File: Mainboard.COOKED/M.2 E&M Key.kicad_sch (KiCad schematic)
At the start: 26 parts, among them J15 Bus_M.2_Socket_M, J16 Bus_M.2_Socket_E

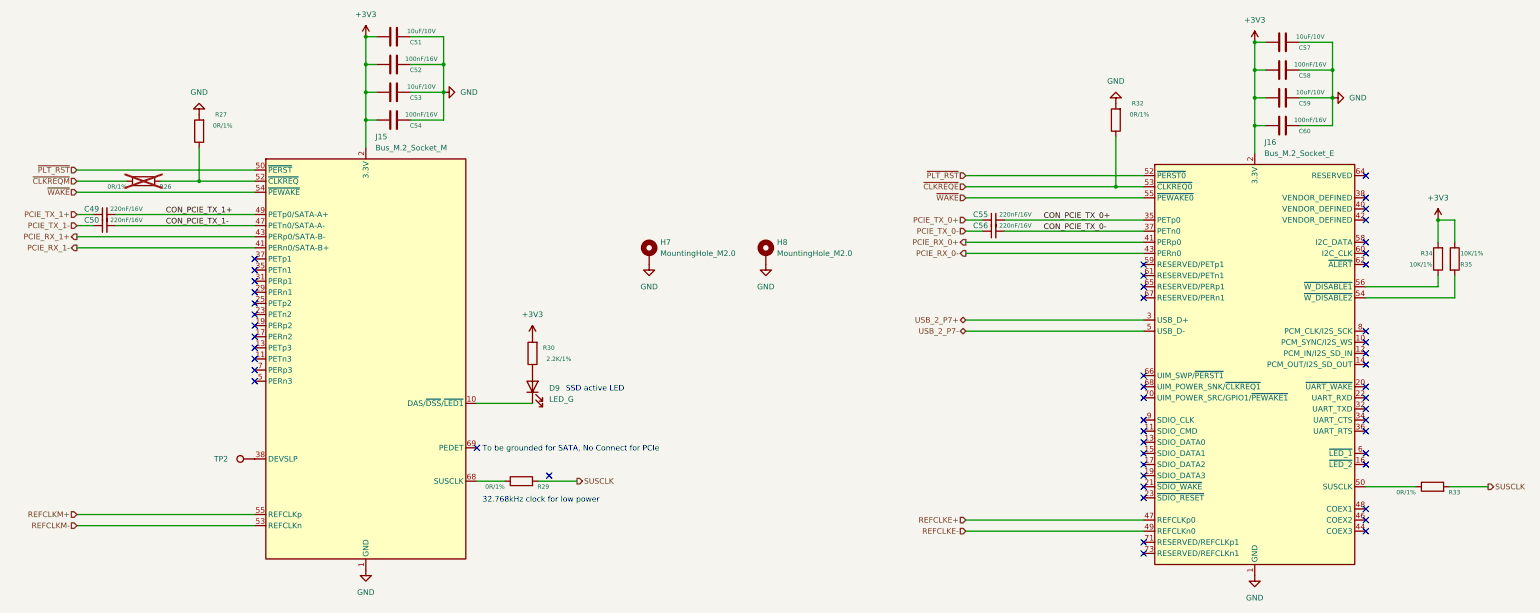
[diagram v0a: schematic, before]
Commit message: "Scrapped" the current Mainboard, seems to be very broken for no reason.
It is being kept for now so that work done for the displays can be copied over later.
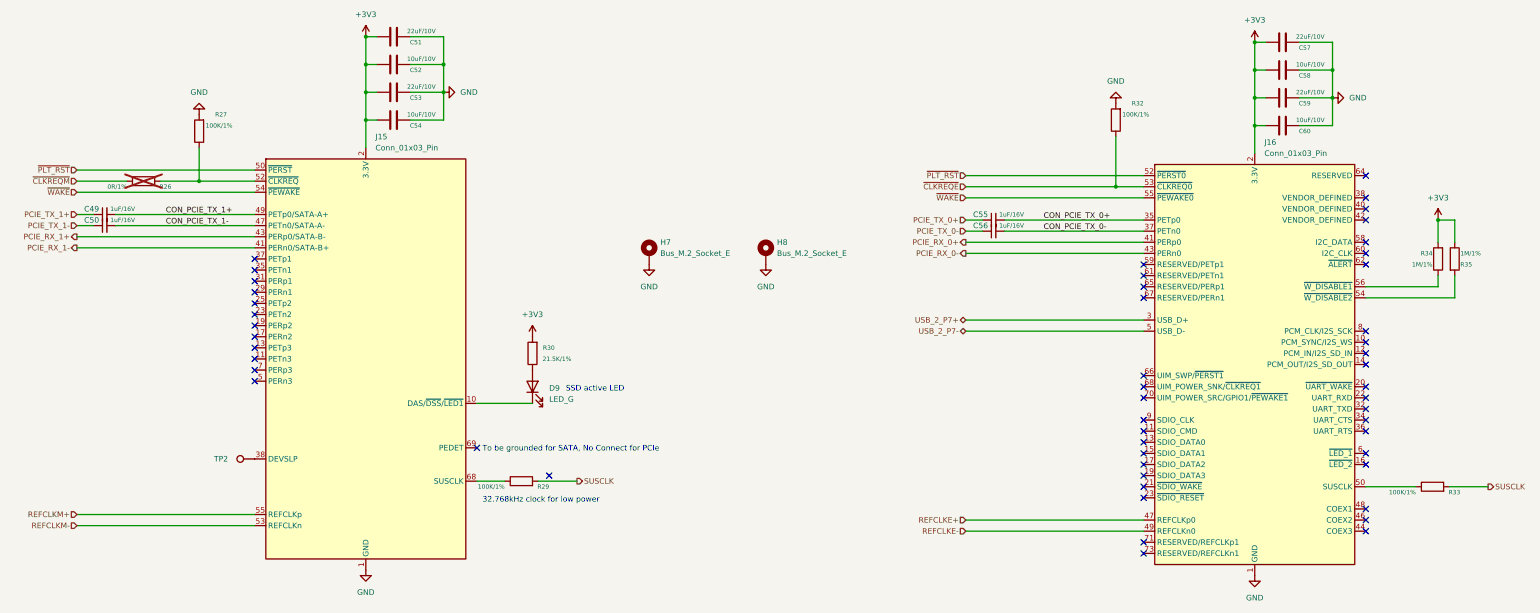
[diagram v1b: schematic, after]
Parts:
- C49, C50, C55, C56: value 220nF/16V -> 1uF/16V; Buy_Link https://item.szlcsc.com/137804.html -> (none); DF_Comment 贴片电容0402-220nF-16V-X7R -> 贴片电容0402-1uF-16V-X5R(0402)
- C51, C53, C57, C59: value 10uF/10V -> 22uF/10V; footprint A_HDJ_Library:C_0402_1005Metric -> A_HDJ_Library:C_0603_1608Metric; DF_Comment 贴片电容0402-10UF-10V-X5R_GRM155R61A106ME44D -> 贴片电容0603-22uF-10V-X5R(0603); SCH_Show_Footprint C0402 -> C603
- C52, C54, C58, C60: value 100nF/16V -> 10uF/10V; DF_Comment 贴片电容0402-100nF-16V-X7R(0402) -> 贴片电容0402-10UF-10V-X5R_GRM155R61A106ME44D; SCH_Show_Footprint C0402 -> -- mixed values --
- D9: DF_Comment 贴片LED蓝色0603(0603) -> 贴片LED红色0603(0603)
- H7, H8: value MountingHole_M2.0 -> Bus_M.2_Socket_E; footprint A_HDJ_Library:MountingHole_2.75mm_M2_4.4mm_Pad_TopOnly -> A_HDJ_Library:PCIe_M.2_Connectors_P=0.5mm_H=4.2mm_KeyE; Buy_Link https://item.taobao.com/item.htm?abbucket=8&id=655855111684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 -> https://item.szlcsc.com/8568583.html; DF_Comment 贴片螺母柱M2XC4X2.5+C2.7X1.5（无铅铜） -> M.2连接器KEY-E_H4.2mm-67P_APCI0108-P001A
- J15: value Bus_M.2_Socket_M -> Conn_01x03_Pin; footprint A_HDJ_Library:PCIe_M.2_Connectors_P=0.5mm_H=4.2mm_KeyM -> A_HDJ_Library:PinHeader_1x03_P2.54mm_Vertical; Buy_Link https://item.szlcsc.com/8568582.html -> (none); DF_Comment M.2连接器KEY-M_H4.2mm-67P_APCI0107-P001A -> 2.54绿色单排排针-3P
- J16: value Bus_M.2_Socket_E -> Conn_01x03_Pin; footprint A_HDJ_Library:PCIe_M.2_Connectors_P=0.5mm_H=4.2mm_KeyE -> A_HDJ_Library:PinHeader_1x03_P2.54mm_Vertical; Buy_Link https://item.szlcsc.com/8568583.html -> (none); DF_Comment M.2连接器KEY-E_H4.2mm-67P_APCI0108-P001A -> 2.54黑色单排排针-3P
- R27, R29, R32, R33: value 0R/1% -> 100K/1%; footprint A_DFRobot:R_0402 -> A_HDJ_Library:R_0402_1005Metric; DF_Comment 贴片电阻0402-0R-1% -> 贴片电阻0402-100K-1%
- R30: value 2.2K/1% -> 21.5K/1%; footprint A_DFRobot:R_0402 -> A_HDJ_Library:R_0402_1005Metric; DF_Comment 贴片电阻0402-2.2K-1% -> 贴片电阻0402-21.5K-1%
- R34, R35: value 10K/1% -> 1M/1%; footprint A_DFRobot:R_0402 -> A_HDJ_Library:R_0402_1005Metric; DF_Comment 贴片电阻0402-10K-1% -> 贴片电阻0402-1M-1%
